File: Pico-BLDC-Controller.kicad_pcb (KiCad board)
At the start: 4 copper layers, 115 x 55 mm, 158 parts, among them J1 Conn_01x10, J2 Heat Mat, J3 I2C CONN, J4 USB_C_Receptacle_USB2.0_14P, J5 SM03B-SRSS-TB, J6 Conn_01x05, J7 Conn_01x02, J8 Conn_01x03, Q1 DMN3053L-7, Q2 SIR680LDP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

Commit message: all
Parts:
- removed the G*** at (119.6, 84.5)
- removed the REF** at (187.4, 93.5)
- removed the REF** at (191.8, 54.1)
- removed the REF** at (191.7, 67.1)
- removed the REF** at (112.5, 47.8)
- removed the REF** at (103.8, 79.6)
- added G***: LOGO, logo:syauqi-logo, B.Cu at (109.6, 76.7)
- added REF**: Symbol_HighVoltage_Triangle_6x6mm_Copper, Symbol:Symbol_HighVoltage_Triangle_6x6mm_Copper, F.Cu at (191.8, 54.8)
- added REF**: OSHW-Logo_5.7x6mm_SilkScreen, Symbol:OSHW-Logo_5.7x6mm_SilkScreen, F.Cu at (112.5, 48.0)
- added REF**: Symbol_HighVoltage_Triangle_6x6mm_Copper, Symbol:Symbol_HighVoltage_Triangle_6x6mm_Copper, F.Cu at (191.6, 67.4)
- added REF**: Symbol_HighVoltage_Triangle_6x6mm_Copper, Symbol:Symbol_HighVoltage_Triangle_6x6mm_Copper, F.Cu at (187.3, 92.4)
- added REF**: OSHW-Logo_5.7x6mm_SilkScreen, Symbol:OSHW-Logo_5.7x6mm_SilkScreen, B.Cu at (117.1, 77.8)
- H1, H2, H3, H4: value MountingHole -> MountingHole_Pad; footprint MountingHole:MountingHole_2.7mm_M2.5_ISO14580 -> MountingHole:MountingHole_2.2mm_M2_DIN965_Pad_TopBottom
- moved H4 116.4 mm to (204.9, 45.6)
- moved H3 113.2 mm to (204.9, 92.6)
- moved H2 106.8 mm to (98.4, 54.1)
- moved H1 106.5 mm to (98.4, 92.6)
- moved REF** 9.80 mm to (113.2, 85.3)
- moved REF** 0.94 mm to (123.1, 59.9)
- moved C42 0.05 mm to (193.9, 55.0)
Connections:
- J8 pad : (no net) -> GND
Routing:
- net VM: vias 299 -> 297
- net /MOTB_OUT: vias 51 -> 50
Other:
- board text added: "DAUGHTER-BOARD"
- board text removed: "DOUGHTER-BOARD"

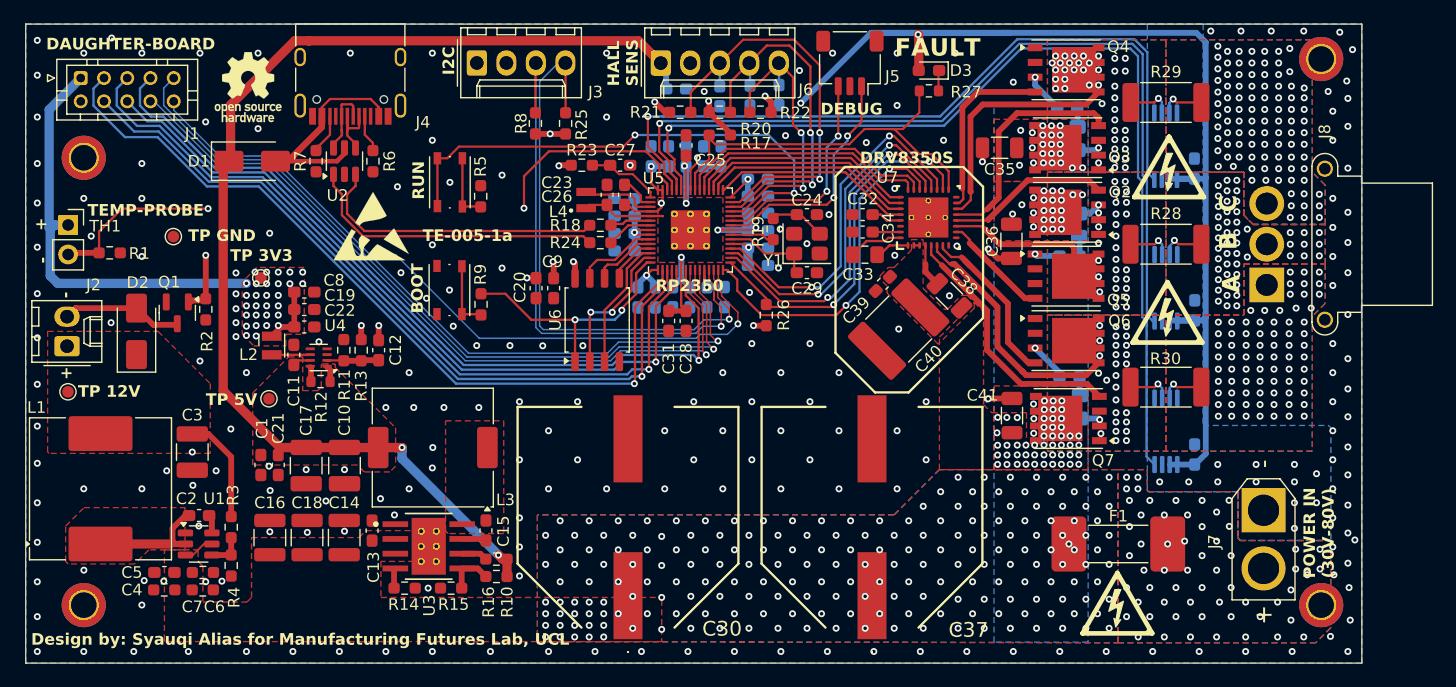
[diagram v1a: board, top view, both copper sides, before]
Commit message: change connector to usb-c
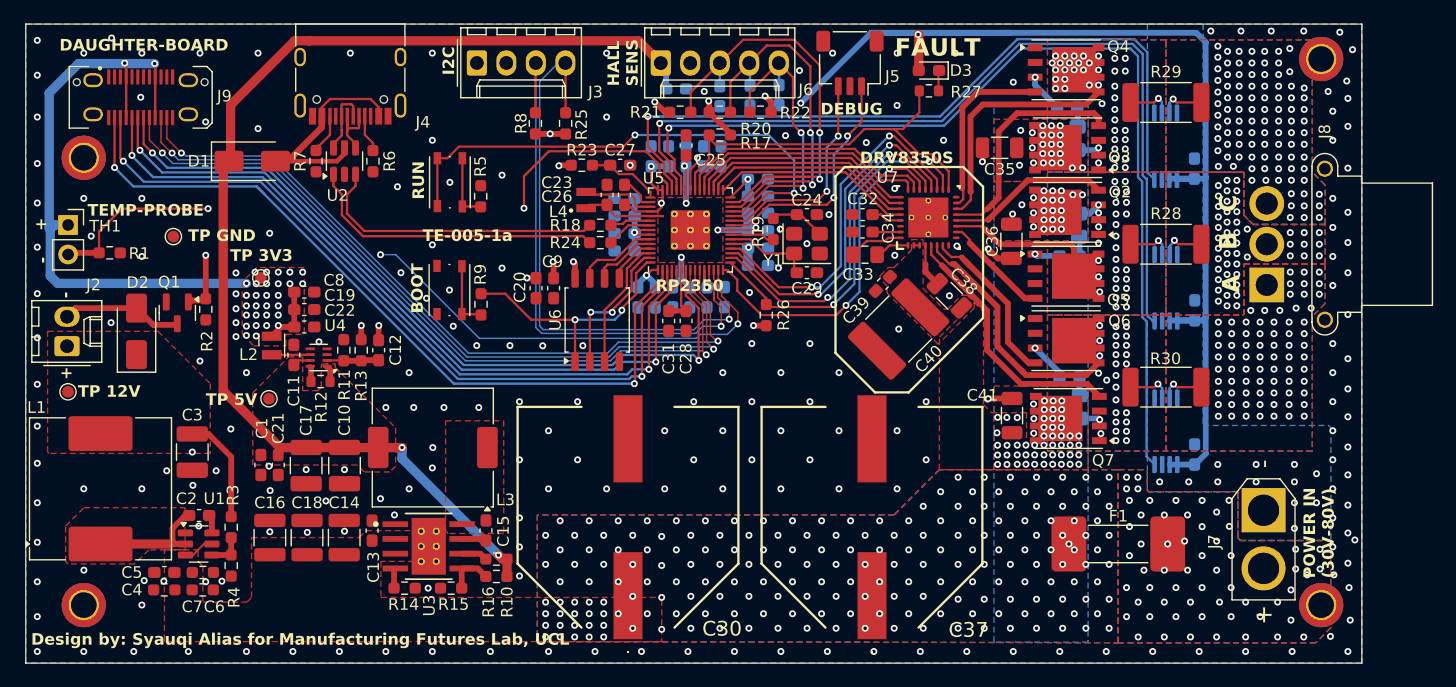
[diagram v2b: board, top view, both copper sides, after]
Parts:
- removed J1: Conn_01x10, Connector_JST:JST_PHD_B10B-PHDSS_2x05_P2.00mm_Vertical
- removed REF** (x3): Symbol_HighVoltage_Triangle_6x6mm_Copper, Symbol:Symbol_HighVoltage_Triangle_6x6mm_Copper
- removed REF** (x2): OSHW-Logo_5.7x6mm_SilkScreen, Symbol:OSHW-Logo_5.7x6mm_SilkScreen
- removed REF**: ESD-Logo_6.6x6mm_SilkScreen, Symbol:ESD-Logo_6.6x6mm_SilkScreen
- removed REF**: KiCad-Logo2_5mm_SilkScreen, Symbol:KiCad-Logo2_5mm_SilkScreen
- added J9: USB_C_Receptacle, Connector_USB:USB_C_Receptacle_JAE_DX07S024WJ3R400, F.Cu at (103.3, 48.9)
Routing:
- net +3V3: track 206.0 -> 223.2 mm, vias 50 -> 52
- net /GPIO2: track 67.7 -> 65.1 mm, vias 1 -> 2
- net /GPIO4: track 68.9 -> 66.7 mm, vias 1 -> 2
- net /CHA_B: track 66.9 -> 65.3 mm, vias 1 -> 2
- net /GPIO0: track 70.0 -> 68.5 mm, vias 1 -> 2
- net /CHA_A: track 65.5 -> 66.1 mm, vias 1 -> 2
- net /GPIO7: track 63.6 -> 64.2 mm, vias 1 -> 2
- net /GPIO1: vias 1 -> 2
- net /GPIO3: vias 1 -> 2

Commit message: update silkscreen
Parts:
- added REF**: Symbol_HighVoltage_Triangle_6x6mm_silkscreen, high_volt:Symbol_HighVoltage_Triangle_6x6mm_silkscreen, F.Cu at (191.5, 67.3)
- added REF**: Symbol_HighVoltage_Triangle_6x6mm_silkscreen, high_volt:Symbol_HighVoltage_Triangle_6x6mm_silkscreen, F.Cu at (187.4, 93.4)
- added REF**: Symbol_HighVoltage_Triangle_6x6mm_silkscreen, high_volt:Symbol_HighVoltage_Triangle_6x6mm_silkscreen, F.Cu at (191.5, 54.8)
- added REF**: ESD-Logo_6.6x6mm_SilkScreen, Symbol:ESD-Logo_6.6x6mm_SilkScreen, F.Cu at (123.3, 60.1)
- added REF**: OSHW-Logo_5.7x6mm_SilkScreen, Symbol:OSHW-Logo_5.7x6mm_SilkScreen, F.Cu at (113.1, 47.8)
- added REF**: OSHW-Logo_5.7x6mm_SilkScreen, Symbol:OSHW-Logo_5.7x6mm_SilkScreen, B.Cu at (125.2, 91.8)
- added REF**: KiCad-Logo2_6mm_SilkScreen, Symbol:KiCad-Logo2_6mm_SilkScreen, B.Cu at (113.1, 91.6)
- added REF**: Symbol_HighVoltage_Triangle_6x6mm_silkscreen, high_volt:Symbol_HighVoltage_Triangle_6x6mm_silkscreen, B.Cu at (200.2, 53.0)
- added REF**: Symbol_HighVoltage_Triangle_6x6mm_silkscreen, high_volt:Symbol_HighVoltage_Triangle_6x6mm_silkscreen, B.Cu at (200.1, 70.0)
- moved G*** 26.8 mm to (131.9, 91.5)
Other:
- board text added: "DC POWER IN (30V-80V)"
- board text added: "OL-005-1a"
- board text removed: "Design by: Syauqi Alias"
- board text removed: "POWER IN (30V-80V)"
- board text removed: "TE-005-1a"

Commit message: all
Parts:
- added REF**: Symbol_HighVoltage_Triangle_6x6mm_silkscreen, high_volt:Symbol_HighVoltage_Triangle_6x6mm_silkscreen, B.Cu at (192.8, 86.9)
- moved REF** 0.40 mm to (112.8, 48.1)
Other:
- board text added: "Si HEAT MAT"
